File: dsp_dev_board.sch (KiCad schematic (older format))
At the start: 26 parts, among them J1 aux_mcu_power, J2 audio_in, J3 audio_out, J4 9v_jack, J5 input_jack, J6 output_jack, U1 TL072, U2 AMS1117-3.3

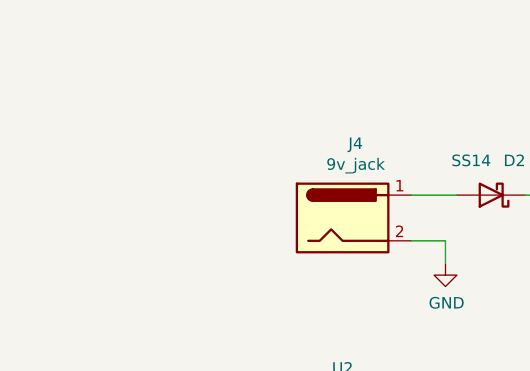
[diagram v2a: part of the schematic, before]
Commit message: Improved probe points
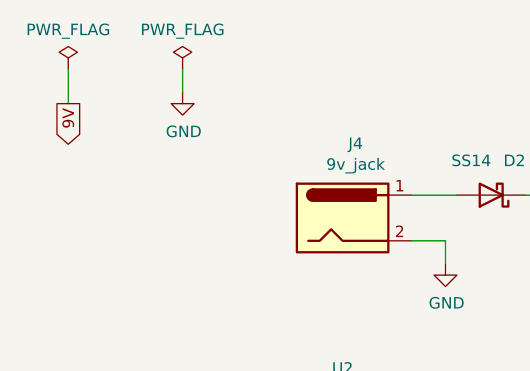
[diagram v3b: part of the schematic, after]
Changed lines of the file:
@@
 $EndComp
 $Comp
-L power:GND #PWR013
+L power:GND #PWR014
 U 1 1 5FFBC04C
 P 9850 2300
-F 0 "#PWR013" H 9850 2050 50  0001 C CNN
+F 0 "#PWR014" H 9850 2050 50  0001 C CNN
 F 1 "GND" H 9855 2127 50  0000 C CNN
 F 2 "" H 9850 2300 50  0001 C CNN
@@
 9V
 $Comp
-L power:GND #PWR07
+L power:GND #PWR08
 U 1 1 60005258
 P 2500 1700
-F 0 "#PWR07" H 2500 1450 50  0001 C CNN
+F 0 "#PWR08" H 2500 1450 50  0001 C CNN
 F 1 "GND" H 2505 1527 50  0000 C CNN
 F 2 "" H 2500 1700 50  0001 C CNN
@@
 	2500 1600 2350 1600
 $Comp
-L power:GND #PWR011
+L power:GND #PWR012
 U 1 1 6002C64C
 P 4700 1300
-F 0 "#PWR011" H 4700 1050 50  0001 C CNN
+F 0 "#PWR012" H 4700 1050 50  0001 C CNN
 F 1 "GND" H 4705 1127 50  0000 C CNN
 F 2 "" H 4700 1300 50  0001 C CNN
@@
 	2150 3950 2150 4050
 $Comp
-L power:GND #PWR03
+L power:GND #PWR04
 U 1 1 600A2818
 P 2150 4500
-F 0 "#PWR03" H 2150 4250 50  0001 C CNN
+F 0 "#PWR04" H 2150 4250 50  0001 C CNN
 F 1 "GND" H 2155 4327 50  0000 C CNN
 F 2 "" H 2150 4500 50  0001 C CNN
@@
 	1500 3550 1500 3700
 $Comp
-L power:GND #PWR01
+L power:GND #PWR02
 U 1 1 600D21C7
 P 1500 4400
-F 0 "#PWR01" H 1500 4150 50  0001 C CNN
+F 0 "#PWR02" H 1500 4150 50  0001 C CNN
 F 1 "GND" H 1505 4227 50  0000 C CNN
 F 2 "" H 1500 4400 50  0001 C CNN
@@
 NoConn ~ 4400 1600
 $Comp
-L power:GND #PWR012
+L power:GND #PWR013
 U 1 1 601D9CA8
 P 4700 2450
-F 0 "#PWR012" H 4700 2200 50  0001 C CNN
+F 0 "#PWR013" H 4700 2200 50  0001 C CNN
 F 1 "GND" H 4705 2277 50  0000 C CNN
 F 2 "" H 4700 2450 50  0001 C CNN
@@
 	2550 2850 2550 2800
 $Comp
-L power:GND #PWR08
+L power:GND #PWR09
 U 1 1 60006D77
 P 2550 2850
-F 0 "#PWR08" H 2550 2600 50  0001 C CNN
+F 0 "#PWR09" H 2550 2600 50  0001 C CNN
 F 1 "GND" H 2555 2677 50  0000 C CNN
 F 2 "" H 2550 2850 50  0001 C CNN
@@
 	2050 2750 2050 2700
 $Comp
-L power:GND #PWR02
+L power:GND #PWR03
 U 1 1 5FFC34F5
 P 2050 2750
-F 0 "#PWR02" H 2050 2500 50  0001 C CNN
+F 0 "#PWR03" H 2050 2500 50  0001 C CNN
 F 1 "GND" H 2055 2577 50  0000 C CNN
 F 2 "" H 2050 2750 50  0001 C CNN
@@
 3.3V
 $Comp
-L power:GND #PWR04
+L power:GND #PWR05
 U 1 1 601E6A36
 P 2150 5750
-F 0 "#PWR04" H 2150 5500 50  0001 C CNN
+F 0 "#PWR05" H 2150 5500 50  0001 C CNN
 F 1 "GND" H 2155 5577 50  0000 C CNN
 F 2 "" H 2150 5750 50  0001 C CNN
@@
 $EndComp
 $Comp
-L power:GND #PWR05
+L power:GND #PWR06
 U 1 1 6026A61A
 P 2150 6350
-F 0 "#PWR05" H 2150 6100 50  0001 C CNN
+F 0 "#PWR06" H 2150 6100 50  0001 C CNN
 F 1 "GND" H 2155 6177 50  0000 C CNN
 F 2 "" H 2150 6350 50  0001 C CNN
@@
 $EndComp
 $Comp
-L power:GND #PWR06
+L power:GND #PWR07
 U 1 1 60272187
 P 2150 7000
-F 0 "#PWR06" H 2150 6750 50  0001 C CNN
+F 0 "#PWR07" H 2150 6750 50  0001 C CNN
 F 1 "GND" H 2155 6827 50  0000 C CNN
 F 2 "" H 2150 7000 50  0001 C CNN
@@
 $EndComp
 $Comp
-L power:GND #PWR09
+L power:GND #PWR010
 U 1 1 600E8A0A
 P 4600 2050
-F 0 "#PWR09" H 4600 1800 50  0001 C CNN
+F 0 "#PWR010" H 4600 1800 50  0001 C CNN
 F 1 "GND" H 4605 1877 50  0000 C CNN
 F 2 "" H 4600 2050 50  0001 C CNN
@@
 $EndComp
 $Comp
-L power:GND #PWR010
+L power:GND #PWR011
 U 1 1 600EC6C0
 P 4600 3200
-F 0 "#PWR010" H 4600 2950 50  0001 C CNN
+F 0 "#PWR011" H 4600 2950 50  0001 C CNN
 F 1 "GND" H 4605 3027 50  0000 C CNN
 F 2 "" H 4600 3200 50  0001 C CNN
@@
 Wire Wire Line
 	2550 1400 2350 1400
+$Comp
+L power:PWR_FLAG #FLG01
+U 1 1 606222E5
+P 850 850
+F 0 "#FLG01" H 850 925 50  0001 C CNN
+F 1 "PWR_FLAG" H 850 1023 50  0000 C CNN
+F 2 "" H 850 850 50  0001 C CNN
+F 3 "~" H 850 850 50  0001 C CNN
+	1    850  850
+	1    0    0    -1
+$EndComp
+Text GLabel 850  1000 3    50   Output ~ 0
+9V
+Wire Wire Line
+	850  1000 850  850
+$Comp
+L power:PWR_FLAG #FLG02
+U 1 1 60625618
+P 1350 850
+F 0 "#FLG02" H 1350 925 50  0001 C CNN
+F 1 "PWR_FLAG" H 1350 1023 50  0000 C CNN
+F 2 "" H 1350 850 50  0001 C CNN
+F 3 "~" H 1350 850 50  0001 C CNN
+	1    1350 850
+	1    0    0    -1
+$EndComp
+$Comp
+L power:GND #PWR01
+U 1 1 60626032
+P 1350 950
+F 0 "#PWR01" H 1350 700 50  0001 C CNN
+F 1 "GND" H 1355 777 50  0000 C CNN
+F 2 "" H 1350 950 50  0001 C CNN
+F 3 "" H 1350 950 50  0001 C CNN
+	1    1350 950
+	1    0    0    -1
+$EndComp
+Wire Wire Line
+	1350 950  1350 850
 $EndSCHEMATC

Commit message: Assign a bunch of footprints
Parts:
- C1, C2, C3, C4, C5: footprint (none) -> Capacitor_SMD:C_0603_1608Metric
- D1, D2, D3, D4: footprint (none) -> Diode_SMD:D_SMA
- J1, J2, J3: footprint (none) -> Connector_PinHeader_2.54mm:PinHeader_1x02_P2.54mm_Vertical
- J4: footprint (none) -> Connector_BarrelJack:BarrelJack_Horizontal
- R1, R2, R3, R4, R5, R6, R7, R8, R9: footprint (none) -> Resistor_SMD:R_0603_1608Metric
- U1: footprint (none) -> Package_SO:SOIC-8_3.9x4.9mm_P1.27mm
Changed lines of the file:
@@
 F 0 "U1" H 8300 2167 50  0000 C CNN
 F 1 "TL072" H 8300 2076 50  0000 C CNN
-F 2 "" H 8300 1800 50  0001 C CNN
+F 2 "Package_SO:SOIC-8_3.9x4.9mm_P1.27mm" H 8300 1800 50  0001 C CNN
 F 3 "http://www.ti.com/lit/ds/symlink/tl071.pdf" H 8300 1800 50  0001 C CNN
 	1    8300 1800
@@
 F 0 "R9" V 9193 1800 50  0000 C CNN
 F 1 "47" V 9284 1800 50  0000 C CNN
-F 2 "" V 9330 1800 50  0001 C CNN
+F 2 "Resistor_SMD:R_0603_1608Metric" V 9330 1800 50  0001 C CNN
 F 3 "~" H 9400 1800 50  0001 C CNN
 	1    9400 1800
@@
 F 0 "D4" V 9804 2129 50  0000 L CNN
 F 1 "SS14" V 9895 2129 50  0000 L CNN
-F 2 "" H 9850 2050 50  0001 C CNN
+F 2 "Diode_SMD:D_SMA" H 9850 2050 50  0001 C CNN
 F 3 "~" H 9850 2050 50  0001 C CNN
 	1    9850 2050
@@
 F 0 "D3" V 9804 1629 50  0000 L CNN
 F 1 "SS14" V 9895 1629 50  0000 L CNN
-F 2 "" H 9850 1550 50  0001 C CNN
+F 2 "Diode_SMD:D_SMA" H 9850 1550 50  0001 C CNN
 F 3 "~" H 9850 1550 50  0001 C CNN
 	1    9850 1550
@@
 F 0 "C4" V 8698 1800 50  0000 C CNN
 F 1 "10u" V 8789 1800 50  0000 C CNN
-F 2 "" H 8988 1650 50  0001 C CNN
+F 2 "Capacitor_SMD:C_0603_1608Metric" H 8988 1650 50  0001 C CNN
 F 3 "~" H 8950 1800 50  0001 C CNN
 	1    8950 1800
@@
 F 0 "J4" H 2107 1825 50  0000 C CNN
 F 1 "9v_jack" H 2107 1734 50  0000 C CNN
-F 2 "" H 2100 1460 50  0001 C CNN
+F 2 "Connector_BarrelJack:BarrelJack_Horizontal" H 2100 1460 50  0001 C CNN
 F 3 "~" H 2100 1460 50  0001 C CNN
 	1    2050 1500
@@
 F 0 "R7" V 8043 2350 50  0000 C CNN
 F 1 "10k" V 8134 2350 50  0000 C CNN
-F 2 "" V 8180 2350 50  0001 C CNN
+F 2 "Resistor_SMD:R_0603_1608Metric" V 8180 2350 50  0001 C CNN
 F 3 "~" H 8250 2350 50  0001 C CNN
 	1    8250 2350
@@
 F 0 "C2" V 6948 1900 50  0000 C CNN
 F 1 "10u" V 7039 1900 50  0000 C CNN
-F 2 "" H 7238 1750 50  0001 C CNN
+F 2 "Capacitor_SMD:C_0603_1608Metric" H 7238 1750 50  0001 C CNN
 F 3 "~" H 7200 1900 50  0001 C CNN
 	1    7200 1900
@@
 F 0 "R1" H 2220 3846 50  0000 L CNN
 F 1 "10k" H 2220 3755 50  0000 L CNN
-F 2 "" V 2080 3800 50  0001 C CNN
+F 2 "Resistor_SMD:R_0603_1608Metric" V 2080 3800 50  0001 C CNN
 F 3 "~" H 2150 3800 50  0001 C CNN
 	1    2150 3800
@@
 F 0 "R2" H 2220 4296 50  0000 L CNN
 F 1 "10k" H 2220 4205 50  0000 L CNN
-F 2 "" V 2080 4250 50  0001 C CNN
+F 2 "Resistor_SMD:R_0603_1608Metric" V 2080 4250 50  0001 C CNN
 F 3 "~" H 2150 4250 50  0001 C CNN
 	1    2150 4250
@@
 F 0 "R5" V 7343 1900 50  0000 C CNN
 F 1 "10k" V 7434 1900 50  0000 C CNN
-F 2 "" V 7480 1900 50  0001 C CNN
+F 2 "Resistor_SMD:R_0603_1608Metric" V 7480 1900 50  0001 C CNN
 F 3 "~" H 7550 1900 50  0001 C CNN
 	1    7550 1900
@@
 F 0 "R8" V 8043 3600 50  0000 C CNN
 F 1 "10k" V 8134 3600 50  0000 C CNN
-F 2 "" V 8180 3600 50  0001 C CNN
+F 2 "Resistor_SMD:R_0603_1608Metric" V 8180 3600 50  0001 C CNN
 F 3 "~" H 8250 3600 50  0001 C CNN
 	1    8250 3600
@@
 F 0 "C3" V 6948 3150 50  0000 C CNN
 F 1 "10u" V 7039 3150 50  0000 C CNN
-F 2 "" H 7238 3000 50  0001 C CNN
+F 2 "Capacitor_SMD:C_0603_1608Metric" H 7238 3000 50  0001 C CNN
 F 3 "~" H 7200 3150 50  0001 C CNN
 	1    7200 3150
@@
 F 0 "R6" V 7343 3150 50  0000 C CNN
 F 1 "10k" V 7434 3150 50  0000 C CNN
-F 2 "" V 7480 3150 50  0001 C CNN
+F 2 "Resistor_SMD:R_0603_1608Metric" V 7480 3150 50  0001 C CNN
 F 3 "~" H 7550 3150 50  0001 C CNN
 	1    7550 3150
@@
 F 0 "U1" H 8300 3417 50  0000 C CNN
 F 1 "TL072" H 8300 3326 50  0000 C CNN
-F 2 "" H 8300 3050 50  0001 C CNN
+F 2 "Package_SO:SOIC-8_3.9x4.9mm_P1.27mm" H 8300 3050 50  0001 C CNN
 F 3 "http://www.ti.com/lit/ds/symlink/tl071.pdf" H 8300 3050 50  0001 C CNN
 	2    8300 3050
@@
 F 0 "U1" H 1558 4046 50  0000 L CNN
 F 1 "TL072" H 1558 3955 50  0000 L CNN
-F 2 "" H 1600 4000 50  0001 C CNN
+F 2 "Package_SO:SOIC-8_3.9x4.9mm_P1.27mm" H 1600 4000 50  0001 C CNN
 F 3 "http://www.ti.com/lit/ds/symlink/tl071.pdf" H 1600 4000 50  0001 C CNN
 	3    1600 4000
@@
 F 0 "C5" V 8698 3050 50  0000 C CNN
 F 1 "10u" V 8789 3050 50  0000 C CNN
-F 2 "" H 8988 2900 50  0001 C CNN
+F 2 "Capacitor_SMD:C_0603_1608Metric" H 8988 2900 50  0001 C CNN
 F 3 "~" H 8950 3050 50  0001 C CNN
 	1    8950 3050
@@
 F 0 "C1" H 2665 2696 50  0000 L CNN
 F 1 "0.1u" H 2665 2605 50  0000 L CNN
-F 2 "" H 2588 2500 50  0001 C CNN
+F 2 "Capacitor_SMD:C_0603_1608Metric" H 2588 2500 50  0001 C CNN
 F 3 "~" H 2550 2650 50  0001 C CNN
 	1    2550 2650
@@
 F 0 "J1" H 1550 5800 50  0000 C CNN
 F 1 "aux_mcu_power" H 1550 5700 50  0000 C CNN
-F 2 "" H 1800 5600 50  0001 C CNN
+F 2 "Connector_PinHeader_2.54mm:PinHeader_1x02_P2.54mm_Vertical" H 1800 5600 50  0001 C CNN
 F 3 "~" H 1800 5600 50  0001 C CNN
 	1    1800 5600
@@
 F 0 "J2" H 1550 6400 50  0000 C CNN
 F 1 "audio_in" H 1550 6300 50  0000 C CNN
-F 2 "" H 1800 6200 50  0001 C CNN
+F 2 "Connector_PinHeader_2.54mm:PinHeader_1x02_P2.54mm_Vertical" H 1800 6200 50  0001 C CNN
 F 3 "~" H 1800 6200 50  0001 C CNN
 	1    1800 6200
@@
 F 0 "J3" H 1550 7050 50  0000 C CNN
 F 1 "audio_out" H 1550 6950 50  0000 C CNN
-F 2 "" H 1800 6850 50  0001 C CNN
+F 2 "Connector_PinHeader_2.54mm:PinHeader_1x02_P2.54mm_Vertical" H 1800 6850 50  0001 C CNN
 F 3 "~" H 1800 6850 50  0001 C CNN
 	1    1800 6850
@@
 F 0 "D1" H 1150 2900 50  0000 L CNN
 F 1 "SS14" H 1300 2900 50  0000 L CNN
-F 2 "" H 1350 2750 50  0001 C CNN
+F 2 "Diode_SMD:D_SMA" H 1350 2750 50  0001 C CNN
 F 3 "~" H 1350 2750 50  0001 C CNN
 	1    1350 2750
@@
 F 0 "R3" H 4670 1896 50  0000 L CNN
 F 1 "1M" H 4670 1805 50  0000 L CNN
-F 2 "" V 4530 1850 50  0001 C CNN
+F 2 "Resistor_SMD:R_0603_1608Metric" V 4530 1850 50  0001 C CNN
 F 3 "~" H 4600 1850 50  0001 C CNN
 	1    4600 1850
@@
 F 0 "R4" H 4670 3046 50  0000 L CNN
 F 1 "1M" H 4670 2955 50  0000 L CNN
-F 2 "" V 4530 3000 50  0001 C CNN
+F 2 "Resistor_SMD:R_0603_1608Metric" V 4530 3000 50  0001 C CNN
 F 3 "~" H 4600 3000 50  0001 C CNN
 	1    4600 3000
@@
 F 0 "D2" H 2550 1250 50  0000 L CNN
 F 1 "SS14" H 2700 1250 50  0000 L CNN
-F 2 "" H 2700 1400 50  0001 C CNN
+F 2 "Diode_SMD:D_SMA" H 2700 1400 50  0001 C CNN
 F 3 "~" H 2700 1400 50  0001 C CNN
 	1    2700 1400

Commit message: just a buncha stuff
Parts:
- C2, C3, C4, C5: value 10u -> 1u; footprint Capacitor_SMD:C_0603_1608Metric -> Capacitor_SMD:C_0805_2012Metric
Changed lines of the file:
@@
 P 8950 1800
 F 0 "C4" V 8698 1800 50  0000 C CNN
-F 1 "10u" V 8789 1800 50  0000 C CNN
-F 2 "Capacitor_SMD:C_0603_1608Metric" H 8988 1650 50  0001 C CNN
+F 1 "1u" V 8789 1800 50  0000 C CNN
+F 2 "Capacitor_SMD:C_0805_2012Metric" H 8988 1650 50  0001 C CNN
 F 3 "~" H 8950 1800 50  0001 C CNN
 	1    8950 1800
@@
 P 7200 1900
 F 0 "C2" V 6948 1900 50  0000 C CNN
-F 1 "10u" V 7039 1900 50  0000 C CNN
-F 2 "Capacitor_SMD:C_0603_1608Metric" H 7238 1750 50  0001 C CNN
+F 1 "1u" V 7039 1900 50  0000 C CNN
+F 2 "Capacitor_SMD:C_0805_2012Metric" H 7238 1750 50  0001 C CNN
 F 3 "~" H 7200 1900 50  0001 C CNN
 	1    7200 1900
@@
 P 7200 3150
 F 0 "C3" V 6948 3150 50  0000 C CNN
-F 1 "10u" V 7039 3150 50  0000 C CNN
-F 2 "Capacitor_SMD:C_0603_1608Metric" H 7238 3000 50  0001 C CNN
+F 1 "1u" V 7039 3150 50  0000 C CNN
+F 2 "Capacitor_SMD:C_0805_2012Metric" H 7238 3000 50  0001 C CNN
 F 3 "~" H 7200 3150 50  0001 C CNN
 	1    7200 3150
@@
 P 8950 3050
 F 0 "C5" V 8698 3050 50  0000 C CNN
-F 1 "10u" V 8789 3050 50  0000 C CNN
-F 2 "Capacitor_SMD:C_0603_1608Metric" H 8988 2900 50  0001 C CNN
+F 1 "1u" V 8789 3050 50  0000 C CNN
+F 2 "Capacitor_SMD:C_0805_2012Metric" H 8988 2900 50  0001 C CNN
 F 3 "~" H 8950 3050 50  0001 C CNN
 	1    8950 3050

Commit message: Progress
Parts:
- U1: footprint Package_SO:SOIC-8_3.9x4.9mm_P1.27mm -> (none)
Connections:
- net at C4.2, R7.1: now also U1.7; no longer U1.1
- net at R5.1, R7.2: now also U1.6 (-); no longer U1.2 (-)
- net at C5.2, R8.1: now also U1.1; no longer U1.7
- net at R6.1, R8.2: now also U1.2 (-); no longer U1.6 (-)
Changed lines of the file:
@@
 $EndDescr
-$Comp
-L Amplifier_Operational:TL072 U1
-U 1 1 5FFB8A7E
-P 8300 1800
-F 0 "U1" H 8300 2167 50  0000 C CNN
-F 1 "TL072" H 8300 2076 50  0000 C CNN
-F 2 "Package_SO:SOIC-8_3.9x4.9mm_P1.27mm" H 8300 1800 50  0001 C CNN
-F 3 "http://www.ti.com/lit/ds/symlink/tl071.pdf" H 8300 1800 50  0001 C CNN
-	1    8300 1800
-	1    0    0    -1
-$EndComp
 $Comp
 L Device:R R9
@@
 Wire Wire Line
 	7950 2950 8000 2950
-$Comp
-L Amplifier_Operational:TL072 U1
-U 2 1 600BA0CD
-P 8300 3050
-F 0 "U1" H 8300 3417 50  0000 C CNN
-F 1 "TL072" H 8300 3326 50  0000 C CNN
-F 2 "Package_SO:SOIC-8_3.9x4.9mm_P1.27mm" H 8300 3050 50  0001 C CNN
-F 3 "http://www.ti.com/lit/ds/symlink/tl071.pdf" H 8300 3050 50  0001 C CNN
-	2    8300 3050
-	1    0    0    -1
-$EndComp
 Text Label 6750 3150 2    50   ~ 0
 audio_out
@@
 Wire Wire Line
 	1350 950  1350 850
+$Comp
+L Amplifier_Operational:TL072 U1
+U 2 1 6045F95D
+P 8300 1800
+F 0 "U1" H 8300 2167 50  0000 C CNN
+F 1 "TL072" H 8300 2076 50  0000 C CNN
+F 2 "" H 8300 1800 50  0001 C CNN
+F 3 "http://www.ti.com/lit/ds/symlink/tl071.pdf" H 8300 1800 50  0001 C CNN
+	2    8300 1800
+	1    0    0    -1
+$EndComp
+$Comp
+L Amplifier_Operational:TL072 U1
+U 1 1 6046444C
+P 8300 3050
+F 0 "U1" H 8300 3417 50  0000 C CNN
+F 1 "TL072" H 8300 3326 50  0000 C CNN
+F 2 "" H 8300 3050 50  0001 C CNN
+F 3 "http://www.ti.com/lit/ds/symlink/tl071.pdf" H 8300 3050 50  0001 C CNN
+	1    8300 3050
+	1    0    0    -1
+$EndComp
 $EndSCHEMATC

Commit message: Basically done?
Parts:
- U1: footprint (none) -> Package_SO:SOIC-8_3.9x4.9mm_P1.27mm
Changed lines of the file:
@@
 F 0 "U1" H 8300 2167 50  0000 C CNN
 F 1 "TL072" H 8300 2076 50  0000 C CNN
-F 2 "" H 8300 1800 50  0001 C CNN
+F 2 "Package_SO:SOIC-8_3.9x4.9mm_P1.27mm" H 8300 1800 50  0001 C CNN
 F 3 "http://www.ti.com/lit/ds/symlink/tl071.pdf" H 8300 1800 50  0001 C CNN
 	2    8300 1800
@@
 F 0 "U1" H 8300 3417 50  0000 C CNN
 F 1 "TL072" H 8300 3326 50  0000 C CNN
-F 2 "" H 8300 3050 50  0001 C CNN
+F 2 "Package_SO:SOIC-8_3.9x4.9mm_P1.27mm" H 8300 3050 50  0001 C CNN
 F 3 "http://www.ti.com/lit/ds/symlink/tl071.pdf" H 8300 3050 50  0001 C CNN
 	1    8300 3050

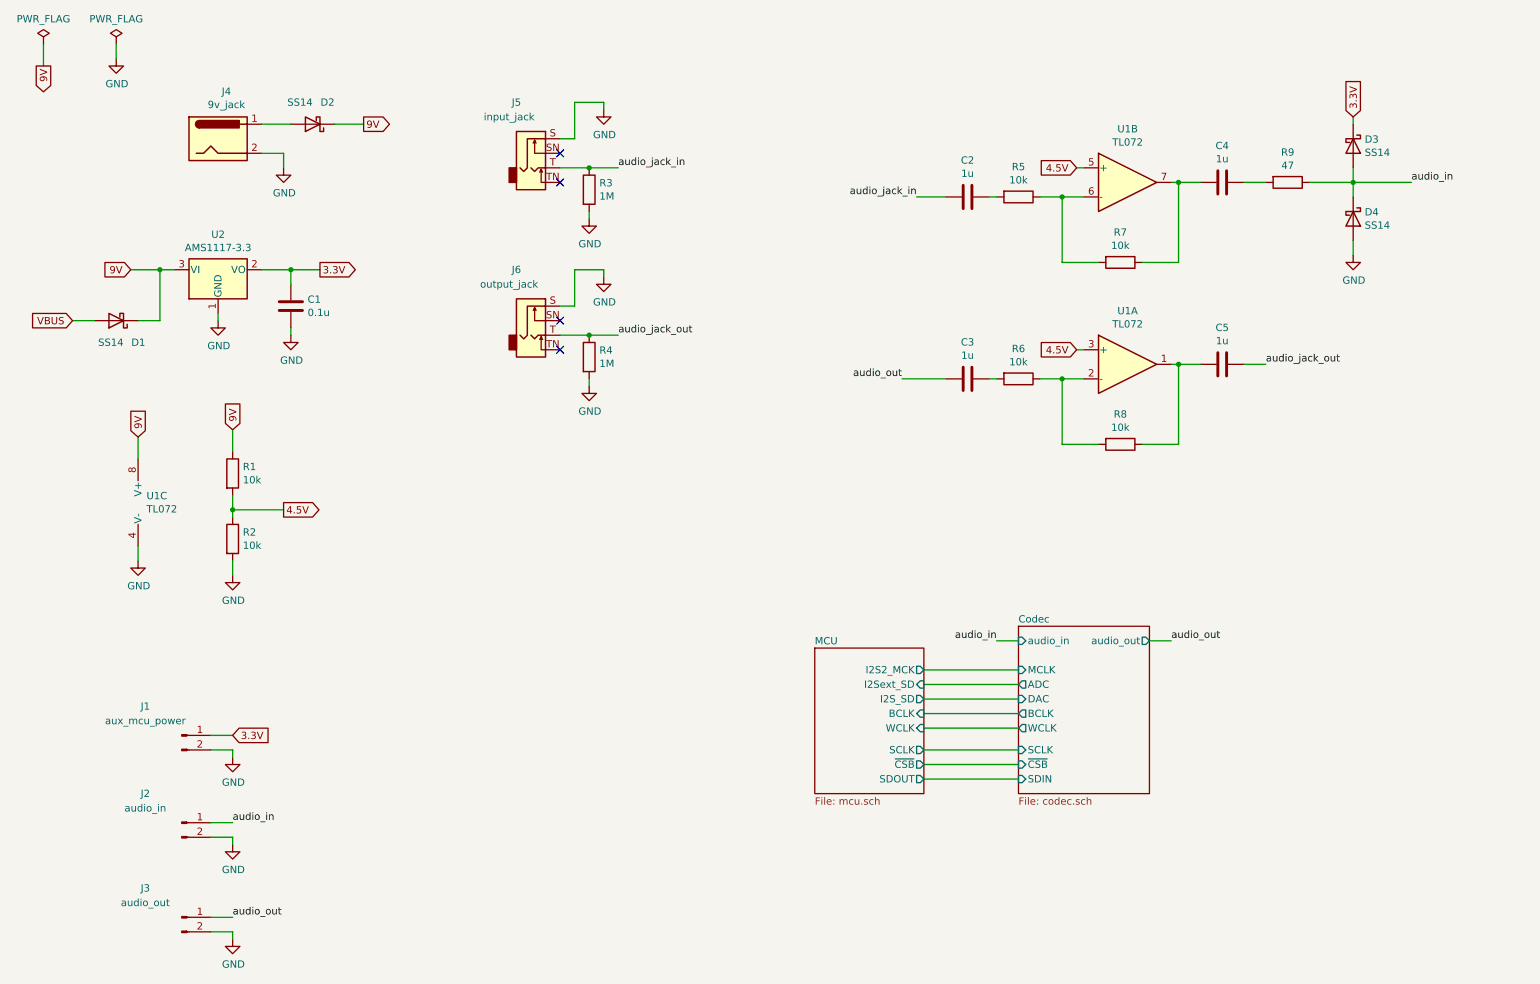
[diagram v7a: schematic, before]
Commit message: Wire up SPI control, add TLV320AIC310x and I2C
The I2C is convenient: if I got it backwards, the SDA and SCL pins are
reversed between SERCOM 2 and 4.
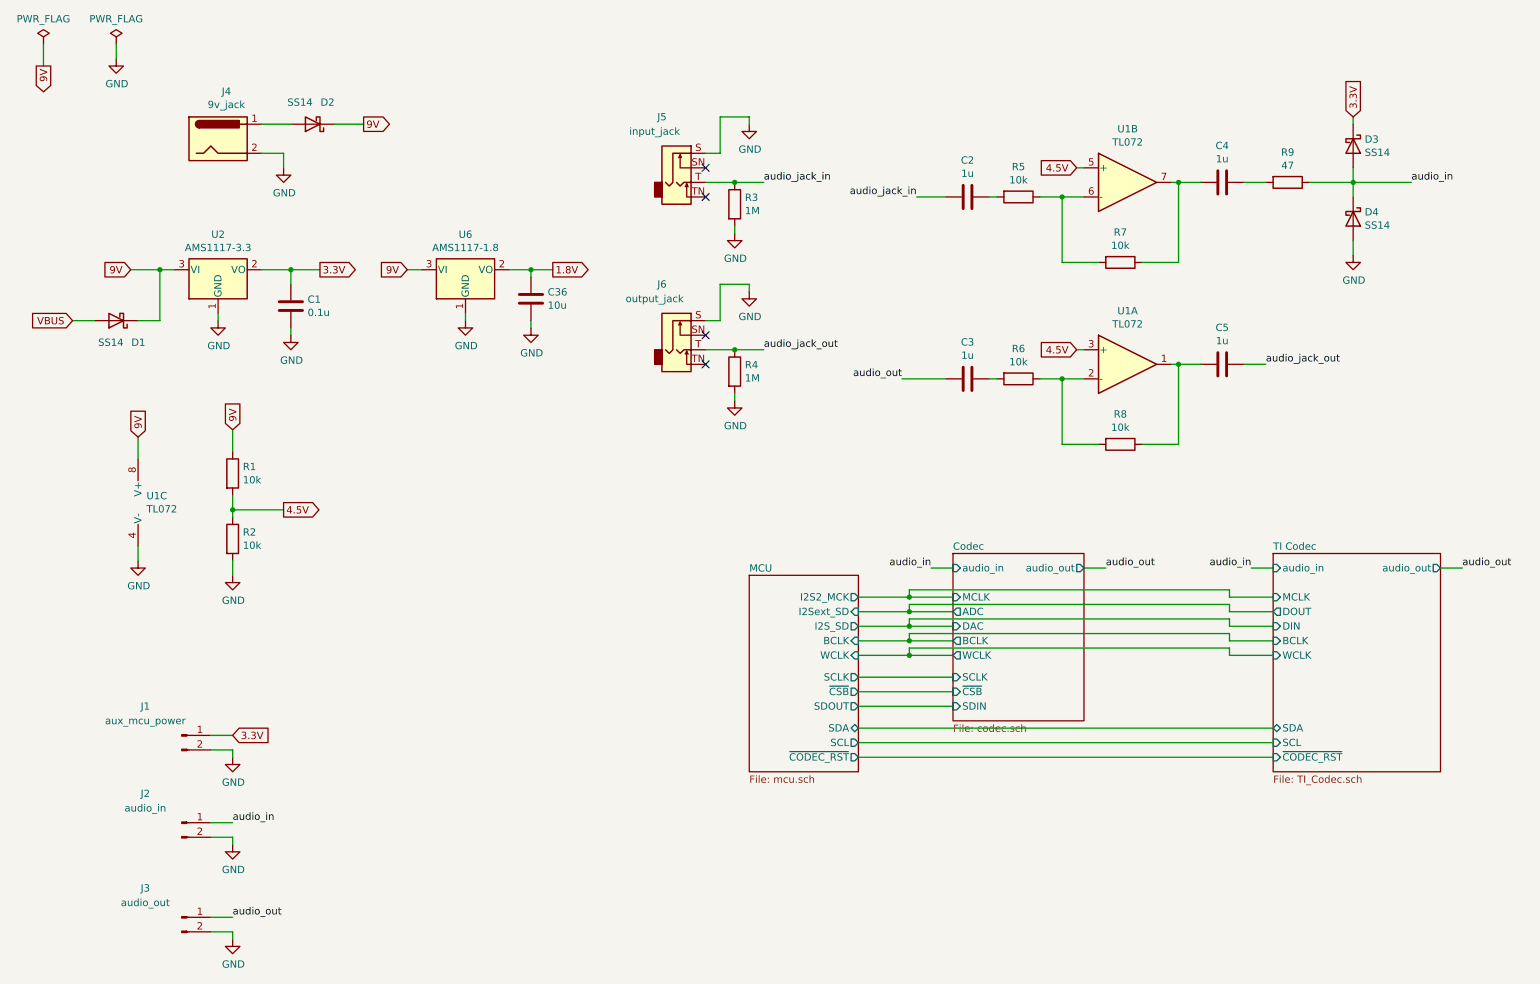
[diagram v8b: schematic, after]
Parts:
- added C36: 10u, Capacitor_SMD:C_0603_1608Metric, symbol Device:C
- added U6: AMS1117-1.8, Package_TO_SOT_SMD:SOT-223-3_TabPin2, symbol Regulator_Linear:AMS1117-1.8
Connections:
- net 9V: now also U6.3 (VI)
- net GND: now also C36.2, U6.1 (GND)
- new net 1.8V: C36.1, U6.2 (VO)
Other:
- moved on the sheet: J5, J6, R3, R4
